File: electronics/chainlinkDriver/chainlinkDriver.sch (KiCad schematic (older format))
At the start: 66 parts, among them J1 Inputs_B, J10 Sensor C, J11 Sensor D, J12 Motor E, J13 Motor F, J14 Sensor E, J15 Sensor F, J16 Power_B, J17 Outputs_A, J18 Outputs_B, J2 Inputs_A, J3 Motor A, J4 Power_A, J5 Motor B, J6 Motor C, J7 Motor D, J8 Sensor A, J9 Sensor B, U1 74HC595, U10 TPL7407L, U2 TPL7407L, U3 74HC125, U4 74HC165, U5 74HC595, U6 TPL7407L, U7 74HC595, U8 TPL7407L, U9 74HC595

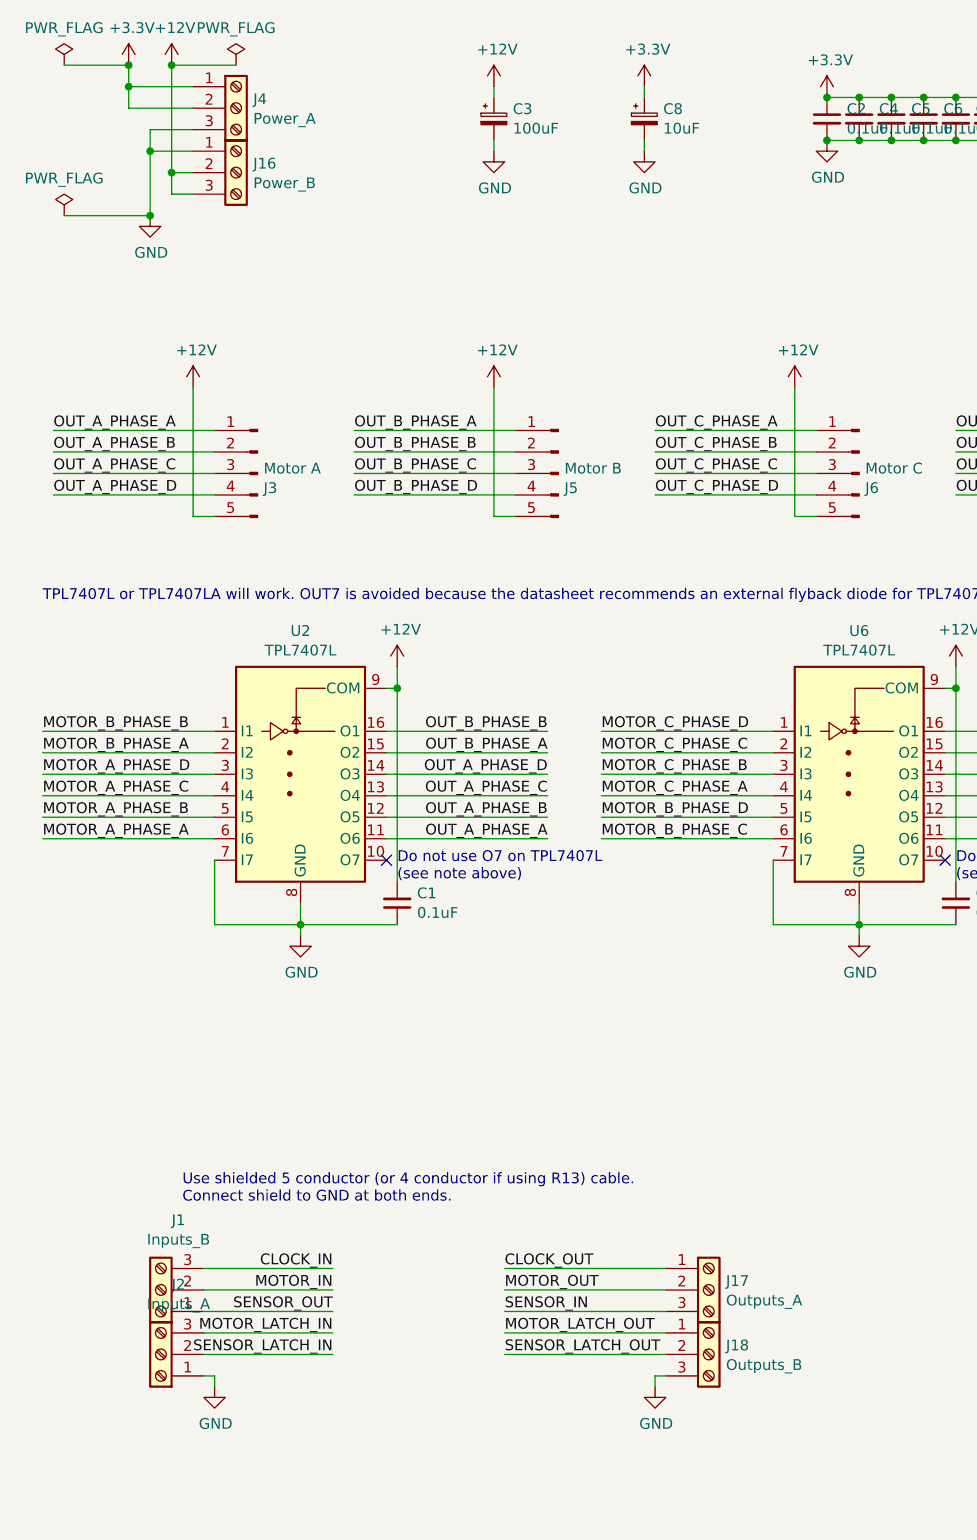
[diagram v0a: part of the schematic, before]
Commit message: Change screw terminals from 3-pin groups to more common 2-pin groups
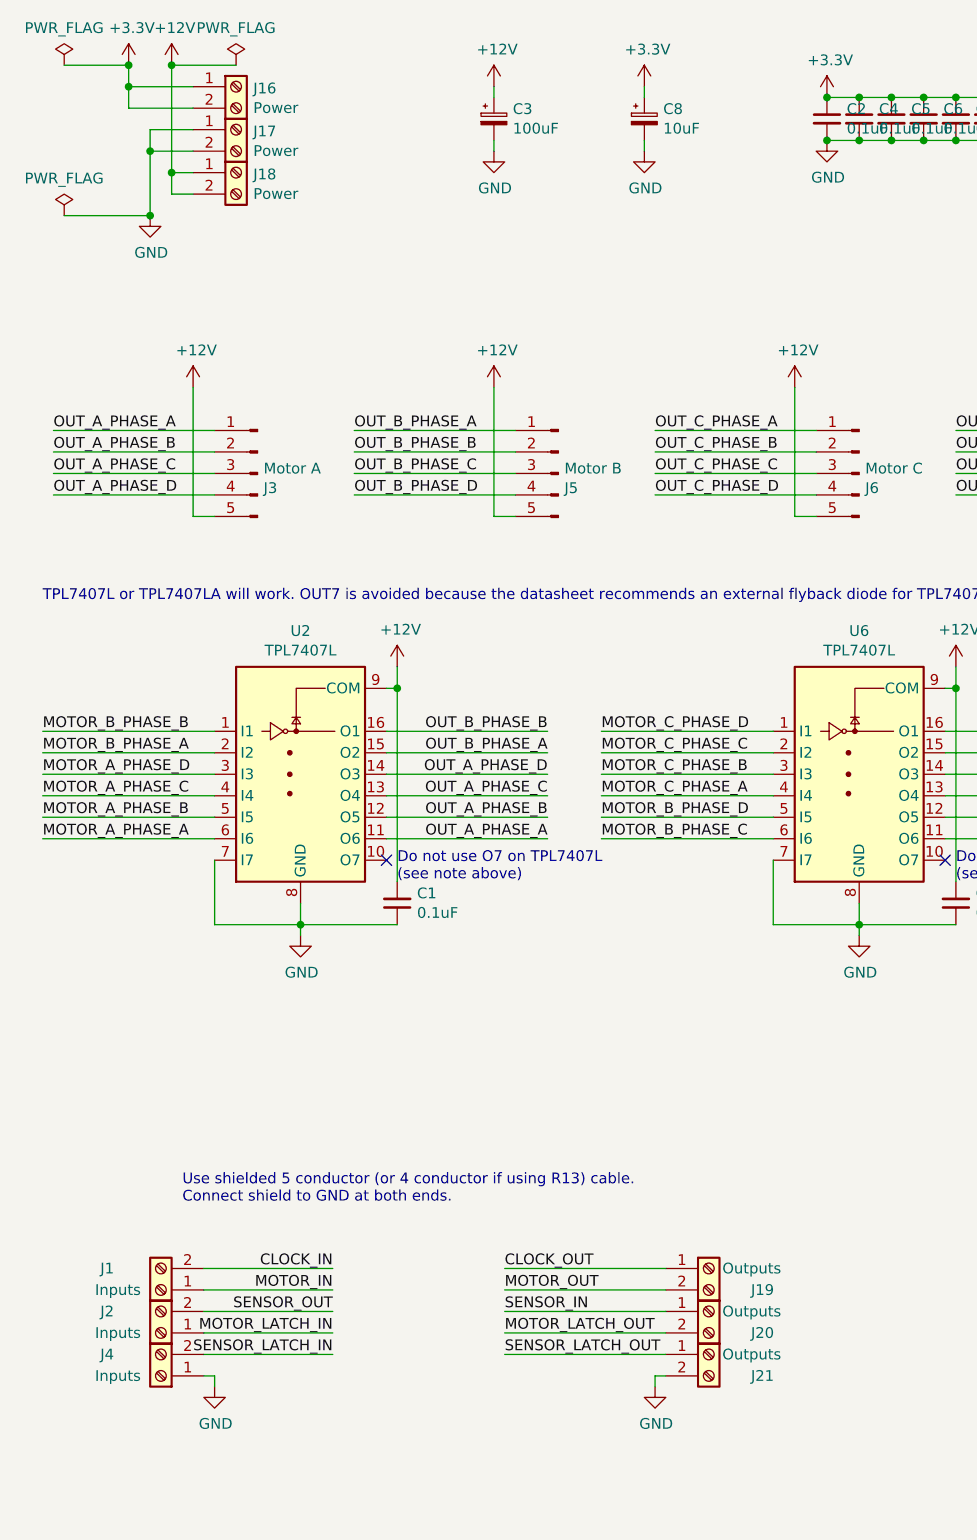
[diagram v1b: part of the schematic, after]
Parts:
- removed J1: Inputs_B, ScrewTerminals:C72334_WJ500V-5.08-3P, symbol Connector:Screw_Terminal_01x03
- removed J16: Power_B, ScrewTerminals:C72334_WJ500V-5.08-3P, symbol Connector:Screw_Terminal_01x03
- removed J17: Outputs_A, ScrewTerminals:C72334_WJ500V-5.08-3P, symbol Connector:Screw_Terminal_01x03
- removed J18: Outputs_B, ScrewTerminals:C72334_WJ500V-5.08-3P, symbol Connector:Screw_Terminal_01x03
- removed J2: Inputs_A, ScrewTerminals:C72334_WJ500V-5.08-3P, symbol Connector:Screw_Terminal_01x03
- removed J4: Power_A, ScrewTerminals:C72334_WJ500V-5.08-3P, symbol Connector:Screw_Terminal_01x03
- added J1, J2, J4: Inputs, ScrewTerminals:C8465_WJ500V-5.08-2P, symbol Connector:Screw_Terminal_01x02
- added J16, J17, J18: Power, ScrewTerminals:C8465_WJ500V-5.08-2P, symbol Connector:Screw_Terminal_01x02
- added J19, J20, J21: Outputs, ScrewTerminals:C8465_WJ500V-5.08-2P, symbol Connector:Screw_Terminal_01x02
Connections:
- net +12V: now also J18.1 (Pin_1), J18.2 (Pin_2)
- net +3V3: now also J16.1 (Pin_1), J16.2 (Pin_2)
- net CLOCK_IN: now also J1.2 (Pin_2)
- net CLOCK_OUT: now also J19.1 (Pin_1)
- net GND: now also J17.1 (Pin_1), J17.2 (Pin_2), J21.2 (Pin_2), J4.1 (Pin_1)
- net MOTOR_IN: now also J1.1 (Pin_1)
- net MOTOR_LATCH_IN: now also J2.1 (Pin_1)
- net MOTOR_LATCH_OUT: now also J20.2 (Pin_2)
- net MOTOR_OUT: now also J19.2 (Pin_2)
- net SENSOR_IN: now also J20.1 (Pin_1)
- net SENSOR_LATCH_IN: now also J4.2 (Pin_2)
- net SENSOR_LATCH_OUT: now also J21.1 (Pin_1)
- net SENSOR_OUT: now also J2.2 (Pin_2)
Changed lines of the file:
@@
 Wire Wire Line
 	9350 6900 9350 7450
-$Comp
-L Connector:Screw_Terminal_01x03 J4
-U 1 1 6100B2D3
-P 1600 1000
-F 0 "J4" H 1680 1042 50  0000 L CNN
-F 1 "Power_A" H 1680 951 50  0000 L CNN
-F 2 "ScrewTerminals:C72334_WJ500V-5.08-3P" H 1600 1000 50  0001 C CNN
-F 3 "~" H 1600 1000 50  0001 C CNN
-F 4 "C72334" H 1600 1000 50  0001 C CNN "LCSC"
-	1    1600 1000
-	1    0    0    -1
-$EndComp
-$Comp
-L Connector:Screw_Terminal_01x03 J16
-U 1 1 6100B87A
-P 1600 1300
-F 0 "J16" H 1680 1342 50  0000 L CNN
-F 1 "Power_B" H 1680 1251 50  0000 L CNN
-F 2 "ScrewTerminals:C72334_WJ500V-5.08-3P" H 1600 1300 50  0001 C CNN
-F 3 "~" H 1600 1300 50  0001 C CNN
-F 4 "C72334" H 1600 1300 50  0001 C CNN "LCSC"
-	1    1600 1300
-	1    0    0    -1
-$EndComp
-$Comp
-L Connector:Screw_Terminal_01x03 J2
-U 1 1 6100DE6D
-P 1250 6800
-F 0 "J2" H 1168 6475 50  0000 C CNN
-F 1 "Inputs_A" H 1168 6566 50  0000 C CNN
-F 2 "ScrewTerminals:C72334_WJ500V-5.08-3P" H 1250 6800 50  0001 C CNN
-F 3 "~" H 1250 6800 50  0001 C CNN
-F 4 "C72334" H 1250 6800 50  0001 C CNN "LCSC"
-	1    1250 6800
-	-1   0    0    1
-$EndComp
-$Comp
-L Connector:Screw_Terminal_01x03 J1
-U 1 1 6106613D
-P 1250 6500
-F 0 "J1" H 1168 6175 50  0000 C CNN
-F 1 "Inputs_B" H 1168 6266 50  0000 C CNN
-F 2 "ScrewTerminals:C72334_WJ500V-5.08-3P" H 1250 6500 50  0001 C CNN
-F 3 "~" H 1250 6500 50  0001 C CNN
-F 4 "C72334" H 1250 6500 50  0001 C CNN "LCSC"
-	1    1250 6500
-	-1   0    0    1
-$EndComp
-$Comp
-L Connector:Screw_Terminal_01x03 J17
-U 1 1 61066781
-P 3800 6500
-F 0 "J17" H 3880 6542 50  0000 L CNN
-F 1 "Outputs_A" H 3880 6451 50  0000 L CNN
-F 2 "ScrewTerminals:C72334_WJ500V-5.08-3P" H 3800 6500 50  0001 C CNN
-F 3 "~" H 3800 6500 50  0001 C CNN
-F 4 "C72334" H 3800 6500 50  0001 C CNN "LCSC"
-	1    3800 6500
-	1    0    0    -1
-$EndComp
-$Comp
-L Connector:Screw_Terminal_01x03 J18
-U 1 1 610B6669
-P 3800 6800
-F 0 "J18" H 3880 6842 50  0000 L CNN
-F 1 "Outputs_B" H 3880 6751 50  0000 L CNN
-F 2 "ScrewTerminals:C72334_WJ500V-5.08-3P" H 3800 6800 50  0001 C CNN
-F 3 "~" H 3800 6800 50  0001 C CNN
-F 4 "C72334" H 3800 6800 50  0001 C CNN "LCSC"
-	1    3800 6800
-	1    0    0    -1
-$EndComp
 NoConn ~ 14800 850
 NoConn ~ 15050 850
@@
 Text Notes 1350 6100 0    50   ~ 0
 Use shielded 5 conductor (or 4 conductor if using R13) cable.\nConnect shield to GND at both ends.
+$Comp
+L Connector:Screw_Terminal_01x02 J16
+U 1 1 604CA397
+P 1600 900
+F 0 "J16" H 1680 892 50  0000 L CNN
+F 1 "Power" H 1680 801 50  0000 L CNN
+F 2 "ScrewTerminals:C8465_WJ500V-5.08-2P" H 1600 900 50  0001 C CNN
+F 3 "~" H 1600 900 50  0001 C CNN
+F 4 "C8465" H 1600 900 50  0001 C CNN "LCSC"
+F 5 "2.40;0;0" H 1600 900 50  0001 C CNN "JLCPCB_CORRECTION"
+	1    1600 900
+	1    0    0    -1
+$EndComp
+$Comp
+L Connector:Screw_Terminal_01x02 J17
+U 1 1 604FD568
+P 1600 1100
+F 0 "J17" H 1680 1092 50  0000 L CNN
+F 1 "Power" H 1680 1001 50  0000 L CNN
+F 2 "ScrewTerminals:C8465_WJ500V-5.08-2P" H 1600 1100 50  0001 C CNN
+F 3 "~" H 1600 1100 50  0001 C CNN
+F 4 "C8465" H 1600 1100 50  0001 C CNN "LCSC"
+F 5 "2.40;0;0" H 1600 1100 50  0001 C CNN "JLCPCB_CORRECTION"
+	1    1600 1100
+	1    0    0    -1
+$EndComp
+$Comp
+L Connector:Screw_Terminal_01x02 J18
+U 1 1 604FD827
+P 1600 1300
+F 0 "J18" H 1680 1292 50  0000 L CNN
+F 1 "Power" H 1680 1201 50  0000 L CNN
+F 2 "ScrewTerminals:C8465_WJ500V-5.08-2P" H 1600 1300 50  0001 C CNN
+F 3 "~" H 1600 1300 50  0001 C CNN
+F 4 "C8465" H 1600 1300 50  0001 C CNN "LCSC"
+F 5 "2.40;0;0" H 1600 1300 50  0001 C CNN "JLCPCB_CORRECTION"
+	1    1600 1300
+	1    0    0    -1
+$EndComp
+$Comp
+L Connector:Screw_Terminal_01x02 J4
+U 1 1 605198F6
+P 1250 6900
+F 0 "J4" H 1500 6800 50  0000 C CNN
+F 1 "Inputs" H 1450 6900 50  0000 C CNN
+F 2 "ScrewTerminals:C8465_WJ500V-5.08-2P" H 1250 6900 50  0001 C CNN
+F 3 "~" H 1250 6900 50  0001 C CNN
+F 4 "C8465" H 1250 6900 50  0001 C CNN "LCSC"
+F 5 "2.40;0;0" H 1250 6900 50  0001 C CNN "JLCPCB_CORRECTION"
+	1    1250 6900
+	-1   0    0    1
+$EndComp
+$Comp
+L Connector:Screw_Terminal_01x02 J2
+U 1 1 6055C477
+P 1250 6700
+F 0 "J2" H 1500 6600 50  0000 C CNN
+F 1 "Inputs" H 1450 6700 50  0000 C CNN
+F 2 "ScrewTerminals:C8465_WJ500V-5.08-2P" H 1250 6700 50  0001 C CNN
+F 3 "~" H 1250 6700 50  0001 C CNN
+F 4 "C8465" H 1250 6700 50  0001 C CNN "LCSC"
+F 5 "2.40;0;0" H 1250 6700 50  0001 C CNN "JLCPCB_CORRECTION"
+	1    1250 6700
+	-1   0    0    1
+$EndComp
+$Comp
+L Connector:Screw_Terminal_01x02 J1
+U 1 1 6055C6FC
+P 1250 6500
+F 0 "J1" H 1500 6400 50  0000 C CNN
+F 1 "Inputs" H 1450 6500 50  0000 C CNN
+F 2 "ScrewTerminals:C8465_WJ500V-5.08-2P" H 1250 6500 50  0001 C CNN
+F 3 "~" H 1250 6500 50  0001 C CNN
+F 4 "C8465" H 1250 6500 50  0001 C CNN "LCSC"
+F 5 "2.40;0;0" H 1250 6500 50  0001 C CNN "JLCPCB_CORRECTION"
+	1    1250 6500
+	-1   0    0    1
+$EndComp
+$Comp
+L Connector:Screw_Terminal_01x02 J19
+U 1 1 6055DB99
+P 3800 6400
+F 0 "J19" H 4050 6300 50  0000 C CNN
+F 1 "Outputs" H 4000 6400 50  0000 C CNN
+F 2 "ScrewTerminals:C8465_WJ500V-5.08-2P" H 3800 6400 50  0001 C CNN
+F 3 "~" H 3800 6400 50  0001 C CNN
+F 4 "C8465" H 3800 6400 50  0001 C CNN "LCSC"
+F 5 "2.40;0;0" H 3800 6400 50  0001 C CNN "JLCPCB_CORRECTION"
+	1    3800 6400
+	1    0    0    -1
+$EndComp
+$Comp
+L Connector:Screw_Terminal_01x02 J20
+U 1 1 6056062F
+P 3800 6600
+F 0 "J20" H 4050 6500 50  0000 C CNN
+F 1 "Outputs" H 4000 6600 50  0000 C CNN
+F 2 "ScrewTerminals:C8465_WJ500V-5.08-2P" H 3800 6600 50  0001 C CNN
+F 3 "~" H 3800 6600 50  0001 C CNN
+F 4 "C8465" H 3800 6600 50  0001 C CNN "LCSC"
+F 5 "2.40;0;0" H 3800 6600 50  0001 C CNN "JLCPCB_CORRECTION"
+	1    3800 6600
+	1    0    0    -1
+$EndComp
+$Comp
+L Connector:Screw_Terminal_01x02 J21
+U 1 1 60560DD4
+P 3800 6800
+F 0 "J21" H 4050 6700 50  0000 C CNN
+F 1 "Outputs" H 4000 6800 50  0000 C CNN
+F 2 "ScrewTerminals:C8465_WJ500V-5.08-2P" H 3800 6800 50  0001 C CNN
+F 3 "~" H 3800 6800 50  0001 C CNN
+F 4 "C8465" H 3800 6800 50  0001 C CNN "LCSC"
+F 5 "2.40;0;0" H 3800 6800 50  0001 C CNN "JLCPCB_CORRECTION"
+	1    3800 6800
+	1    0    0    -1
+$EndComp
 $EndSCHEMATC

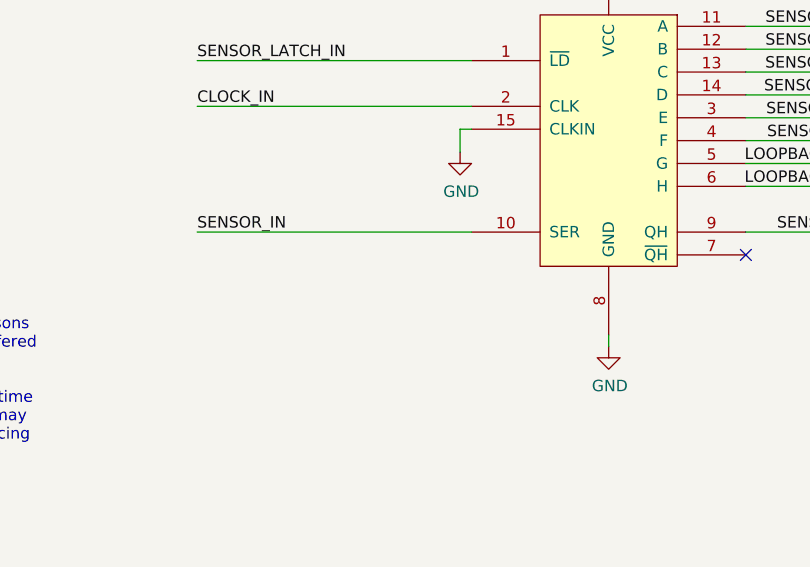
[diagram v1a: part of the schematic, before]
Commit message: chainlinkDriver: add sensor input pulldown, change shield terminal label from GND to SHD
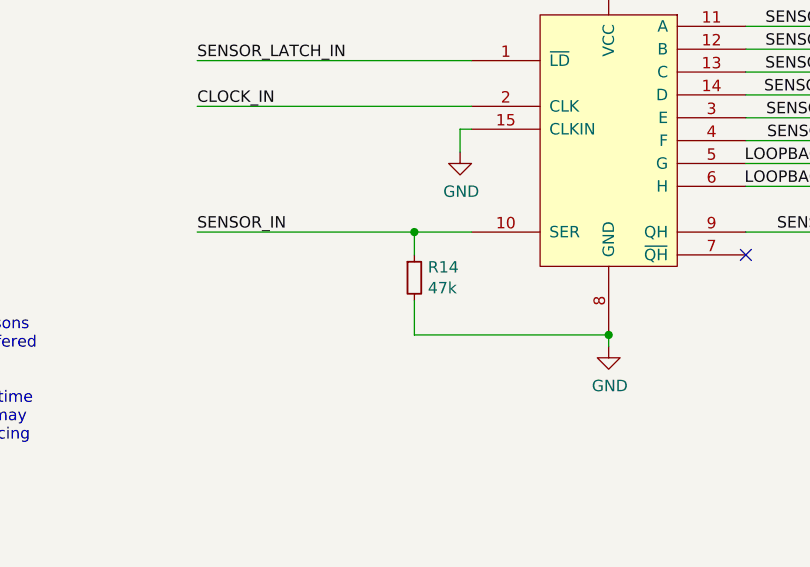
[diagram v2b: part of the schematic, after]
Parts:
- added R14: 47k, Resistor_SMD:R_0603_1608Metric, symbol Device:R_Small
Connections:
- net GND: now also R14.2
- net SENSOR_IN: now also R14.1
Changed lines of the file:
@@
 Connection ~ 1200 1500
 Wire Wire Line
-	13250 6550 14450 6550
+	13250 6550 14200 6550
 Wire Wire Line
 	700  4300 1500 4300
@@
 	1    0    0    -1
 $EndComp
+$Comp
+L Device:R_Small R14
+U 1 1 60866A83
+P 14200 6750
+F 0 "R14" H 14259 6796 50  0000 L CNN
+F 1 "47k" H 14259 6705 50  0000 L CNN
+F 2 "Resistor_SMD:R_0603_1608Metric" H 14200 6750 50  0001 C CNN
+F 3 "~" H 14200 6750 50  0001 C CNN
+F 4 "C25819" H 14200 6750 50  0001 C CNN "LCSC"
+	1    14200 6750
+	1    0    0    -1
+$EndComp
+Wire Wire Line
+	14200 6550 14200 6650
+Connection ~ 14200 6550
+Wire Wire Line
+	14200 6550 14450 6550
+Wire Wire Line
+	14200 6850 14200 7000
+Wire Wire Line
+	14200 7000 15050 7000
+Connection ~ 15050 7000
 $EndSCHEMATC
